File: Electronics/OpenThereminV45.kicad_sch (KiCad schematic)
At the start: 99 parts, among them J2 Conn_02x03_Odd_Even, J3 Conn_02x05_Odd_Even, J4 PJ-320B, J5 PJ-320B, J6 USB_C_Receptacle_USB2.0_16P, P1 10k, P10 BUTTON, P11 A3_PAD, P12 A2_PAD, P13 A1_PAD, P14 A0_PAD, P16 GND, P2 10k, P3 10k, P4 10k, P8 VCC, P9 GND, U1 TTP223, U10 CH340C, U11 LP2985-3.3, U12 MCP4922-E/SL, U2 74HC4060D, U3 74HC4060D, U4 74HC74, U5 HEF4069, U6 MCP4921-E/SN, U7 MCP4922-E/SL, U8 MCP6002T-I/SN, U9 ATmega328P-AU, X1 16MHz, X2 7.3728MHz, Y1 Pitch, Y2 Volume

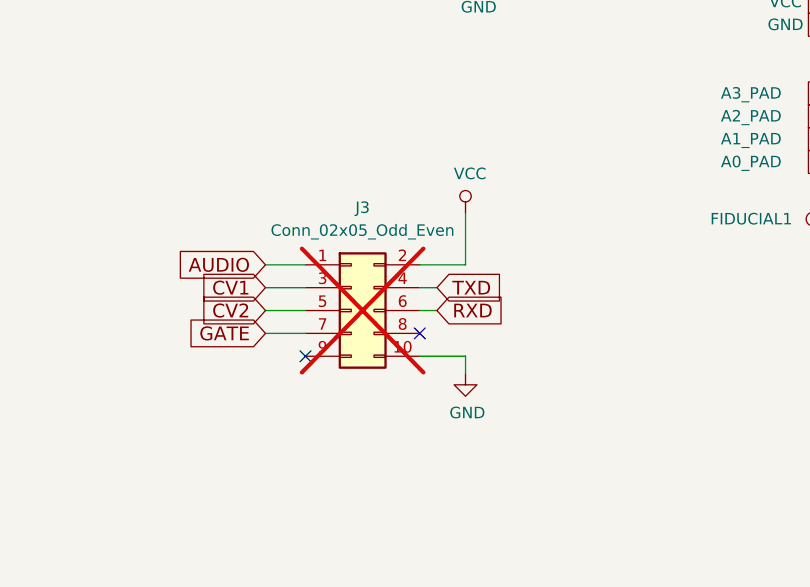
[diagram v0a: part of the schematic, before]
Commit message: Replace 02x05 pin connector with 02x04
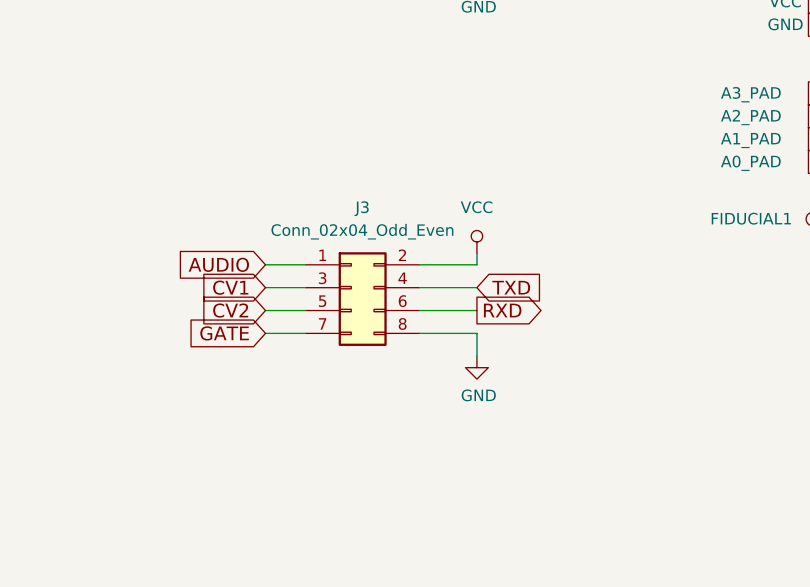
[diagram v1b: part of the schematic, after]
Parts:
- removed J3: Conn_02x05_Odd_Even, Connector_PinHeader_1.27mm:PinHeader_2x05_P1.27mm_Vertical_SMD, symbol Connector_Generic:Conn_02x05_Odd_Even
- added J3: Conn_02x04_Odd_Even, Connector_PinHeader_1.27mm:PinHeader_2x04_P1.27mm_Vertical_SMD, symbol Connector_Generic:Conn_02x04_Odd_Even
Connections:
- net AUDIO: now also J3.1 (Pin_1)
- net CV1: now also J3.3 (Pin_3)
- net CV2: now also J3.5 (Pin_5)
- net GATE: now also J3.7 (Pin_7)
- net GND: now also J3.8 (Pin_8)
- net RXD: now also J3.6 (Pin_6)
- net TXD: now also J3.4 (Pin_4)
- net VCC: now also J3.2 (Pin_2)
- no-connect marks 37 -> 35
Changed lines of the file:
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@@
 	)
 	(no_connect
-		(at 464.82 350.52)
-	)
-	(no_connect
 		(at 156.21 55.88)
 	)
@@
 	)
 	(no_connect
-		(at 477.52 347.98)
-	)
-	(no_connect
 		(at 459.74 204.47)
 	)
@@
 	(wire
 		(pts
-			(xy 477.52 340.36) (xy 482.6 340.36)
+			(xy 477.52 340.36) (xy 483.87 340.36)
 		)
 		(stroke
@@
 	(wire
 		(pts
-			(xy 477.52 342.9) (xy 479.425 342.9)
-		)
-		(stroke
-			(width 0)
-			(type default)
-		)
-	)
-	(wire
-		(pts
 			(xy 81.28 238.76) (xy 81.28 236.22)
 		)
@@
 	(wire
 		(pts
-			(xy 477.52 345.44) (xy 479.425 345.44)
-		)
-		(stroke
-			(width 0)
-			(type default)
-		)
-	)
-	(wire
-		(pts
 			(xy 463.55 201.93) (xy 459.74 201.93)
 		)
@@
 	(wire
 		(pts
+			(xy 483.87 342.9) (xy 477.52 342.9)
+		)
+		(stroke
+			(width 0)
+			(type default)
+		)
+	)
+	(wire
+		(pts
 			(xy 506.73 38.1) (xy 494.03 38.1)
 		)
@@
 	(wire
 		(pts
-			(xy 477.52 350.52) (xy 482.6 350.52)
+			(xy 477.52 347.98) (xy 483.87 347.98)
 		)
 		(stroke
@@
 	(wire
 		(pts
+			(xy 483.87 339.09) (xy 483.87 340.36)
+		)
+		(stroke
+			(width 0)
+			(type default)
+		)
+	)
+	(wire
+		(pts
 			(xy 60.96 71.12) (xy 60.96 72.39)
 		)
@@
 	(wire
 		(pts
+			(xy 483.87 345.44) (xy 477.52 345.44)
+		)
+		(stroke
+			(width 0)
+			(type default)
+		)
+	)
+	(wire
+		(pts
 			(xy 137.16 125.73) (xy 157.48 125.73)
 		)
@@
 	(wire
 		(pts
-			(xy 482.6 340.36) (xy 482.6 334.645)
-		)
-		(stroke
-			(width 0)
-			(type default)
-		)
-	)
-	(wire
-		(pts
 			(xy 323.85 367.03) (xy 332.74 367.03)
 		)
@@
 	(wire
 		(pts
-			(xy 482.6 350.52) (xy 482.6 352.425)
+			(xy 483.87 347.98) (xy 483.87 350.52)
 		)
 		(stroke
@@
 	(global_label "TXD"
 		(shape input)
-		(at 479.425 342.9 0)
+		(at 483.87 342.9 0)
 		(fields_autoplaced yes)
 		(effects
@@
 		)
 		(property "Intersheetrefs" "${INTERSHEET_REFS}"
-			(at 211.455 151.13 0)
+			(at 215.9 151.13 0)
 			(effects
 				(font
@@
 	)
 	(global_label "RXD"
-		(shape input)
-		(at 479.425 345.44 0)
+		(shape output)
+		(at 483.87 345.44 0)
 		(fields_autoplaced yes)
 		(effects
@@
 		)
 		(property "Intersheetrefs" "${INTERSHEET_REFS}"
-			(at 211.455 151.13 0)
+			(at 215.9 151.13 0)
 			(effects
 				(font
@@
 	)
 	(symbol
-		(lib_id "Connector_Generic:Conn_02x05_Odd_Even")
-		(at 469.9 345.44 0)
-		(unit 1)
-		(exclude_from_sim no)
-		(in_bom yes)
-		(on_board yes)
-		(dnp yes)
-		(fields_autoplaced yes)
-		(property "Reference" "J3"
-			(at 471.17 334.01 0)
-			(effects
-				(font
-					(size 1.27 1.27)
-				)
-			)
-		)
-		(property "Value" "Conn_02x05_Odd_Even"
-			(at 471.17 336.55 0)
-			(effects
-				(font
-					(size 1.27 1.27)
-				)
-			)
-		)
-		(property "Footprint" "Connector_PinHeader_1.27mm:PinHeader_2x05_P1.27mm_Vertical_SMD"
-			(at 469.9 345.44 0)
-			(effects
-				(font
-					(size 1.27 1.27)
-				)
-				(hide yes)
-			)
-		)
-		(property "Datasheet" "~"
-			(at 469.9 345.44 0)
-			(effects
-				(font
-					(size 1.27 1.27)
-				)
-				(hide yes)
-			)
-		)
-		(property "Description" ""
-			(at 469.9 345.44 0)
-			(effects
-				(font
-					(size 1.27 1.27)
-				)
-				(hide yes)
-			)
-		)
-		(property "Note" ""
-			(at 469.9 345.44 0)
-			(effects
-				(font
-					(size 1.27 1.27)
-				)
-				(hide yes)
-			)
-		)
-		(pin "1"
-		)
-		(pin "10"
-		)
-		(pin "2"
-		)
-		(pin "3"
-		)
-		(pin "4"
-		)
-		(pin "5"
-		)
-		(pin "6"
-		)
-		(pin "7"
-		)
-		(pin "8"
-		)
-		(pin "9"
-		)
-		(instances
-			(project ""
-				(path "/e6f05f4b-c6f7-49e9-850f-9a638923ab53"
-					(reference "J3")
-					(unit 1)
-				)
-			)
-		)
-	)
-	(symbol
 		(lib_id "Connector:USB_C_Receptacle_USB2.0_16P")
 		(at 518.16 190.5 0)
@@
 	(symbol
 		(lib_id "OpenThereminV41-rescue:VCC-OpenThereminV4-rescue")
-		(at 482.6 334.645 0)
+		(at 483.87 339.09 0)
 		(unit 1)
 		(exclude_from_sim no)
@@
 		(on_board yes)
 		(dnp no)
+		(fields_autoplaced yes)
 		(property "Reference" "#PWR0128"
-			(at 482.6 338.455 0)
+			(at 483.87 342.9 0)
 			(effects
 				(font
@@
 		)
 		(property "Value" "VCC"
-			(at 483.108 330.2508 0)
+			(at 483.87 334.01 0)
 			(effects
 				(font
@@
 		)
 		(property "Footprint" ""
-			(at 482.6 334.645 0)
+			(at 483.87 339.09 0)
 			(effects
 				(font
@@
 		)
 		(property "Datasheet" ""
-			(at 482.6 334.645 0)
+			(at 483.87 339.09 0)
 			(effects
 				(font
@@
 		)
 		(property "Description" ""
-			(at 482.6 334.645 0)
+			(at 483.87 339.09 0)
 			(effects
 				(font
@@
 	(symbol
 		(lib_id "OpenThereminV41-rescue:GND-OpenThereminV4-rescue")
-		(at 482.6 352.425 0)
+		(at 483.87 350.52 0)
 		(unit 1)
 		(exclude_from_sim no)
@@
 		(dnp no)
 		(property "Reference" "#PWR0129"
-			(at 482.6 358.775 0)
+			(at 483.87 356.87 0)
 			(effects
 				(font
@@
 		)
 		(property "Value" "GND"
-			(at 482.8032 356.8192 0)
+			(at 484.0732 354.9142 0)
 			(effects
 				(font
@@
 		)
 		(property "Footprint" ""
-			(at 482.6 352.425 0)
+			(at 483.87 350.52 0)
 			(effects
 				(font
@@
 		)
 		(property "Datasheet" ""
-			(at 482.6 352.425 0)
+			(at 483.87 350.52 0)
 			(effects
 				(font
@@
 		)
 		(property "Description" ""
-			(at 482.6 352.425 0)
+			(at 483.87 350.52 0)
 			(effects
 				(font
@@
 					(unit 1)
 				)
+			)
+		)
+	)
+	(symbol
+		(lib_id "Connector_Generic:Conn_02x04_Odd_Even")
+		(at 469.9 342.9 0)
+		(unit 1)
+		(exclude_from_sim no)
+		(in_bom yes)
+		(on_board yes)
+		(dnp no)
+		(fields_autoplaced yes)
+		(property "Reference" "J3"
+			(at 471.17 334.01 0)
+			(effects
+				(font
+					(size 1.27 1.27)
+				)
+			)
+		)
+		(property "Value" "Conn_02x04_Odd_Even"
+			(at 471.17 336.55 0)
+			(effects
+				(font
+					(size 1.27 1.27)
+				)
+			)
+		)
+		(property "Footprint" "Connector_PinHeader_1.27mm:PinHeader_2x04_P1.27mm_Vertical_SMD"
+			(at 469.9 342.9 0)
+			(effects
+				(font
+					(size 1.27 1.27)
+				)
+				(hide yes)
+			)
+		)
+		(property "Datasheet" "~"
+			(at 469.9 342.9 0)
+			(effects
+				(font
+					(size 1.27 1.27)
+				)
+				(hide yes)
+			)
+		)
+		(property "Description" "Generic connector, double row, 02x04, odd/even pin numbering scheme (row 1 odd numbers, row 2 even numbers), script generated (kicad-library-utils/schlib/autogen/connector/)"
+			(at 469.9 342.9 0)
+			(effects
+				(font
+					(size 1.27 1.27)
+				)
+				(hide yes)
+			)
+		)
+		(property "LCSC" "C27985144"
+			(at 469.9 342.9 0)
+			(effects
+				(font
+					(size 1.27 1.27)
+				)
+				(hide yes)
+			)
+		)
+		(property "PN" "HC-PZ127-7.2L-2x3PS"
+			(at 469.9 342.9 0)
+			(effects
+				(font
+					(size 1.27 1.27)
+				)
+				(hide yes)
+			)
+		)
+		(property "Vendor" "HC"
+			(at 469.9 342.9 0)
+			(effects
+				(font
+					(size 1.27 1.27)
+				)
+				(hide yes)
+			)
+		)
+		(pin "1"
+		)
+		(pin "8"
+		)
+		(pin "6"
+		)
+		(pin "4"
+		)
+		(pin "3"
+		)
+		(pin "7"
+		)
+		(pin "5"
+		)
+		(pin "2"
+		)
+		(instances
+			(project ""
+				(path "/e6f05f4b-c6f7-49e9-850f-9a638923ab53"
+					(reference "J3")
+					(unit 1)
+				)

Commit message: Set component info for ANT connector
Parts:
- Y1, Y2: LCSC (none) -> C5301788; Note (none) -> L=4mm; PN (none) -> SMTSOM340STR; Vendor (none) -> Yiyuan; now in the parts list
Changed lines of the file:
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@@
 		(unit 1)
 		(exclude_from_sim no)
-		(in_bom no)
+		(in_bom yes)
 		(on_board yes)
 		(dnp no)
@@
 			)
 		)
-		(property "Note" ""
+		(property "Note" "L=4mm"
+			(at 43.18 50.8 0)
+			(effects
+				(font
+					(size 1.27 1.27)
+				)
+				(hide yes)
+			)
+		)
+		(property "LCSC" "C5301788"
+			(at 43.18 50.8 0)
+			(effects
+				(font
+					(size 1.27 1.27)
+				)
+				(hide yes)
+			)
+		)
+		(property "PN" "SMTSOM340STR"
+			(at 43.18 50.8 0)
+			(effects
+				(font
+					(size 1.27 1.27)
+				)
+				(hide yes)
+			)
+		)
+		(property "Vendor" "Yiyuan"
 			(at 43.18 50.8 0)
 			(effects
@@
 		(unit 1)
 		(exclude_from_sim no)
-		(in_bom no)
+		(in_bom yes)
 		(on_board yes)
 		(dnp no)
@@
 			)
 		)
-		(property "Note" ""
+		(property "Note" "L=4mm"
+			(at 43.18 143.51 0)
+			(effects
+				(font
+					(size 1.27 1.27)
+				)
+				(hide yes)
+			)
+		)
+		(property "LCSC" "C5301788"
+			(at 43.18 143.51 0)
+			(effects
+				(font
+					(size 1.27 1.27)
+				)
+				(hide yes)
+			)
+		)
+		(property "PN" "SMTSOM340STR"
+			(at 43.18 143.51 0)
+			(effects
+				(font
+					(size 1.27 1.27)
+				)
+				(hide yes)
+			)
+		)
+		(property "Vendor" "Yiyuan"
 			(at 43.18 143.51 0)
 			(effects

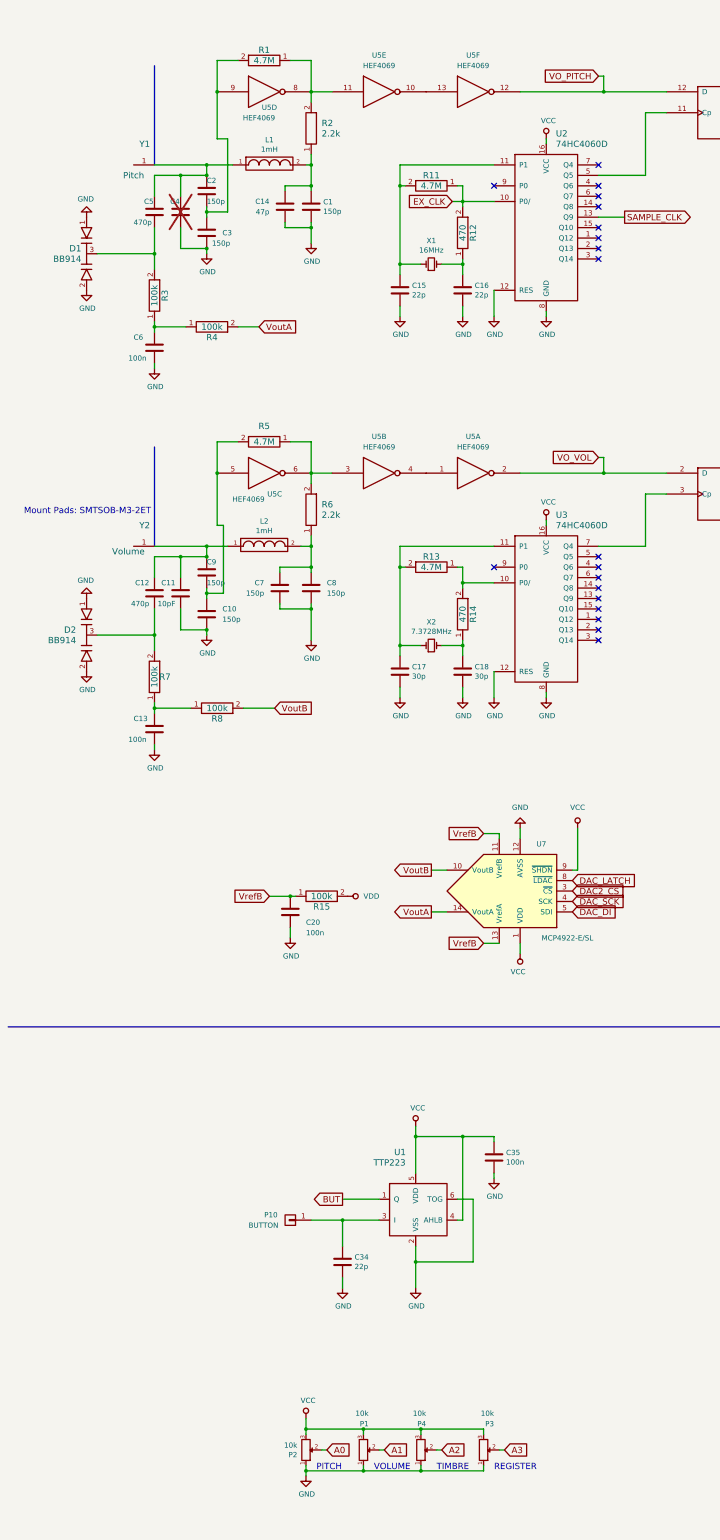
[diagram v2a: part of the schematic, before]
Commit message: Update schema & layout
- Use SMA as antenna connector
- Replace potentiometers with cheaper & higher avaliability option
- Re-route some of the traces
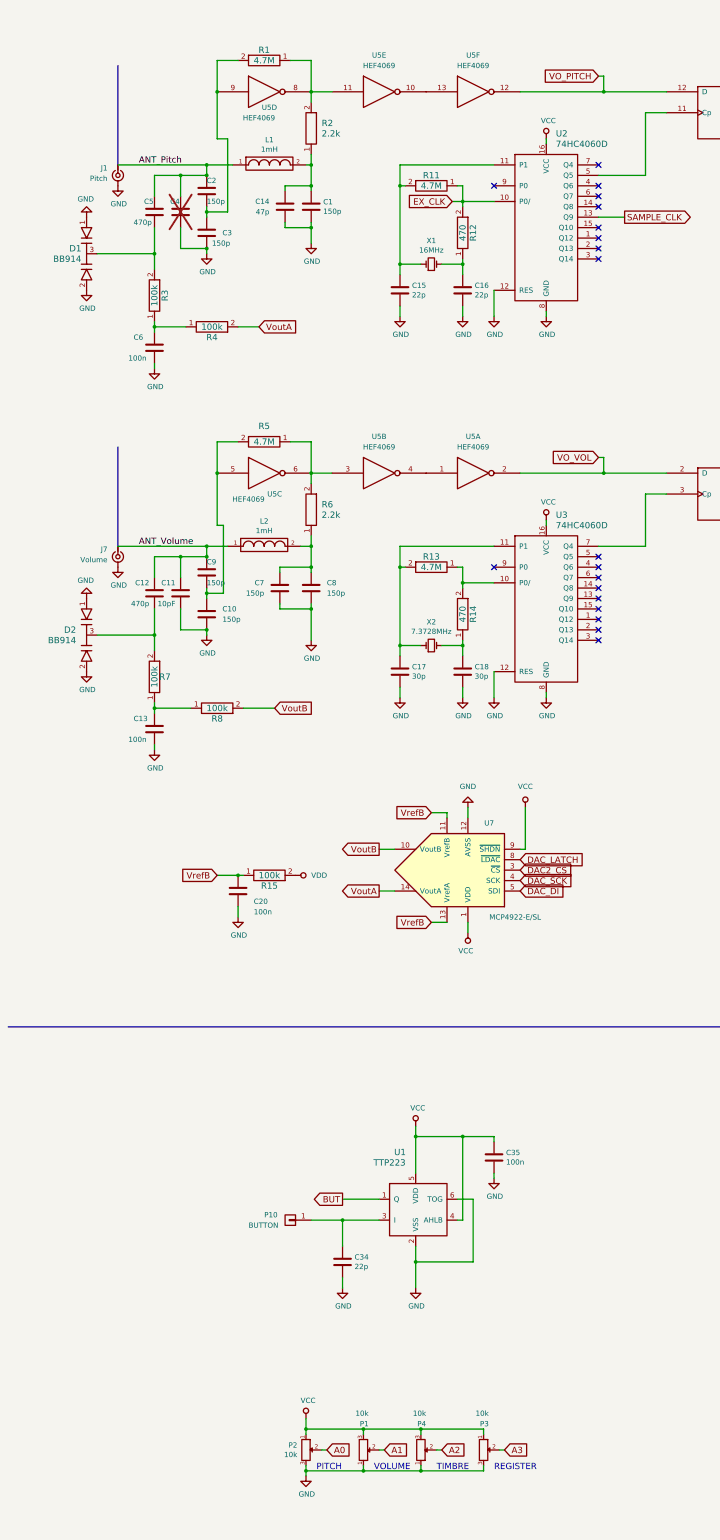
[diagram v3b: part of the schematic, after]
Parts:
- removed Y1: Pitch, GaudiLabsFootPrints:SMTSOB_M3, symbol OpenThereminV41-rescue:MountPad3-OpenThereminV4-rescue
- removed Y2: Volume, GaudiLabsFootPrints:SMTSOB_M3, symbol OpenThereminV41-rescue:MountPad3-OpenThereminV4-rescue
- added J1: Pitch, Connector_Coaxial:SMA_Amphenol_132134-11_Vertical, symbol Connector:Conn_Coaxial_Small
- added J7: Volume, Connector_Coaxial:SMA_Amphenol_132134-11_Vertical, symbol Connector:Conn_Coaxial_Small
- P1, P2, P3, P4: footprint GaudiLabsFootPrints:PS15NV60 -> Library:ALPS_RK09K1130A6S; LCSC C5848081 -> C209770; PN PS15NV60-103A3030 -> RK09K1130A6S; Vendor Amphenol -> ALPS
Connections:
- net GND: now also P2.3, P3.3, J1.2 (Ext), J7.2 (Ext); no longer P2.1, P3.1
- net VCC: now also P2.1, P3.1; no longer P2.3, P3.3
- net ANT_Pitch: now reaches C2.1, C4.1, C5.1, L1.1
- net ANT_Pitch: now also J1.1 (In)
- net ANT_Volume: now reaches C11.1, C12.1, C9.1, L2.1
- net ANT_Volume: now also J7.1 (In)
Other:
- note removed: "Mount Pads: SMTSOB-M3-2ET"
- moved on the sheet: C20, R15, U7

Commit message: Correct 2x4 pin header part info
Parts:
- J3: LCSC C27985144 -> C19268845; PN HC-PZ127-7.2L-2x3PS -> XDZ127-2-04-S-1.0-G1; Vendor HC -> XUNDA
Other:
- note added: "0.7328KHz"
- note added: "1.6MHz"
- note added: "Sample & Hold"
- note added: "Sample clock - Pitch"
- note added: "Sample clock - Vol"
- moved on the sheet: D1, D2
